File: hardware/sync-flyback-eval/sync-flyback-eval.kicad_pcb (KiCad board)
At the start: 2 copper layers, 90.8 x 46.4 mm, 97 parts, among them J1 RJ45_LED_Shielded, Q1 SiR422DP, Q2 Si7898DP, Q3 MMDT3906, T1 PoE_Transformer, T2 Pulse_Transformer, U1 TPS23754PWPR, U2 TCMT1107

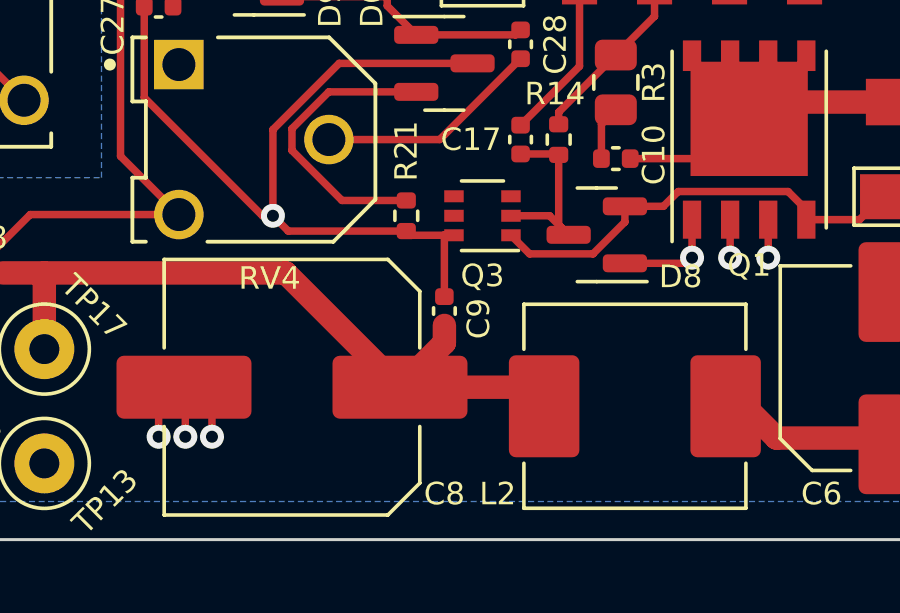
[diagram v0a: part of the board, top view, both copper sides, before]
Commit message: flyback: shift C9 to provide a bit more clearance
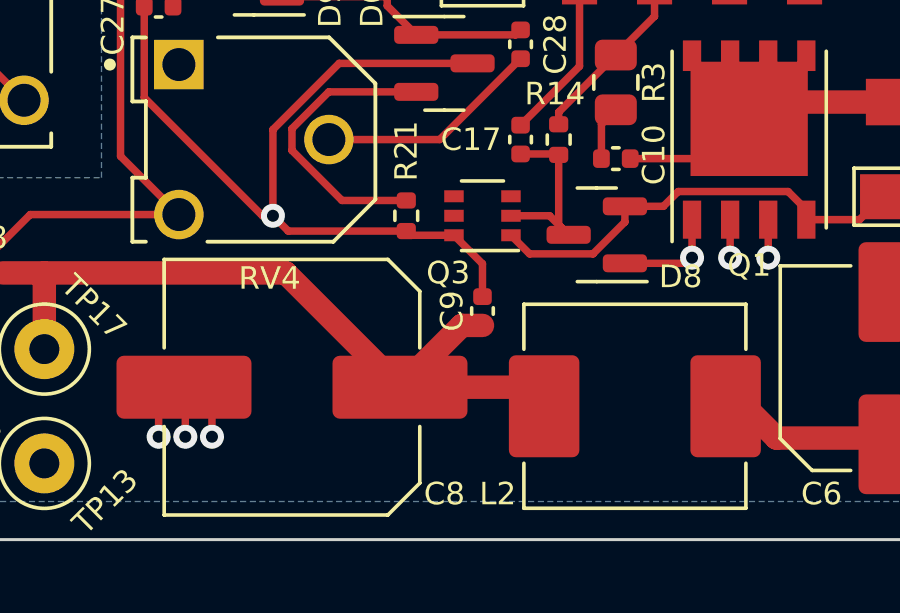
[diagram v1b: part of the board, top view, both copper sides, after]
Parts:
- moved C9 1.27 mm to (160.0, 113.0)
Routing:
- net Net-(C8-Pad1): track 24.8 -> 25.8 mm
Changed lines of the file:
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@@
   )
   (footprint "Capacitor_SMD:C_0402_1005Metric" (layer "F.Cu")
-    (at 158.75 113.03 90)
+    (at 160.02 113.03 90)
     (descr "Capacitor SMD 0402 (1005 Metric), square (rectangular) end terminal, IPC_7351 nominal, (Body size source: IPC-SM-782 page 76, https://www.pcb-3d.com/wordpress/wp-content/uploads/ipc-sm-782a_amendment_1_and_2.pdf), generated with kicad-footprint-generator")
     (tags "capacitor")
@@
     (property "Voltage" "16V")
     (attr smd)
-    (fp_text reference "C9" (at -0.254 1.143 90) (layer "F.SilkS")
+    (fp_text reference "C9" (at 0 -1.016 90) (layer "F.SilkS")
       (effects (font (size 0.75 0.75) (thickness 0.1)))
     )
@@
     (property "Sheetname" "")
     (attr smd)
-    (fp_text reference "Q3" (at 0 -2) (layer "F.SilkS")
+    (fp_text reference "Q3" (at 1.143 -1.905) (layer "F.SilkS")
       (effects (font (size 0.75 0.75) (thickness 0.1)))
     )
@@
   (segment (start 157.48 110.365) (end 153.545 110.365) (width 0.25) (layer "F.Cu") (net 5))
   (segment (start 164.135 100.235) (end 165.755 101.855) (width 0.25) (layer "F.Cu") (net 5))
+  (segment (start 160.02 112.55) (end 160.02 111.455) (width 0.25) (layer "F.Cu") (net 5))
   (segment (start 157.48 110.365) (end 157.62 110.505) (width 0.25) (layer "F.Cu") (net 5))
+  (segment (start 160.02 111.455) (end 159.07 110.505) (width 0.25) (layer "F.Cu") (net 5))
   (segment (start 148.745 102.87) (end 148.745 105.914622) (width 0.25) (layer "F.Cu") (net 5))
-  (segment (start 158.75 112.55) (end 158.75 110.49) (width 0.25) (layer "F.Cu") (net 5))
   (segment (start 157.62 110.505) (end 159.07 110.505) (width 0.25) (layer "F.Cu") (net 5))
   (segment (start 159.6875 104.775) (end 155.241418 104.775) (width 0.25) (layer "F.Cu") (net 5))
@@
   (segment (start 140.690028 85.09) (end 140.690028 83.57) (width 0.25) (layer "F.Cu") (net 63))
   (segment (start 144.160011 88.1888) (end 144.160011 87.391011) (width 0.25) (layer "F.Cu") (net 63))
-  (segment (start 157.27 115.57) (end 158.75 114.09) (width 0.781439) (layer "F.Cu") (net 64))
+  (segment (start 160.02 113.51) (end 159.33 113.51) (width 0.781439) (layer "F.Cu") (net 64))
+  (segment (start 159.33 113.51) (end 157.27 115.57) (width 0.781439) (layer "F.Cu") (net 64))
   (segment (start 145.415 114.3) (end 145.415 111.76) (width 0.781439) (layer "F.Cu") (net 64))
   (segment (start 153.46 111.76) (end 144.02 111.76) (width 0.781439) (layer "F.Cu") (net 64))
   (segment (start 157.27 115.57) (end 153.46 111.76) (width 0.781439) (layer "F.Cu") (net 64))
   (segment (start 157.27 115.57) (end 162.075 115.57) (width 0.781439) (layer "F.Cu") (net 64))
-  (segment (start 158.75 114.09) (end 158.75 113.51) (width 0.781439) (layer "F.Cu") (net 64))
   (segment (start 116.715 77.47) (end 116.715 78.74) (width 0.25) (layer "F.Cu") (net 65))
   (segment (start 116.73 77.47) (end 118.11 77.47) (width 0.25) (layer "F.Cu") (net 65))

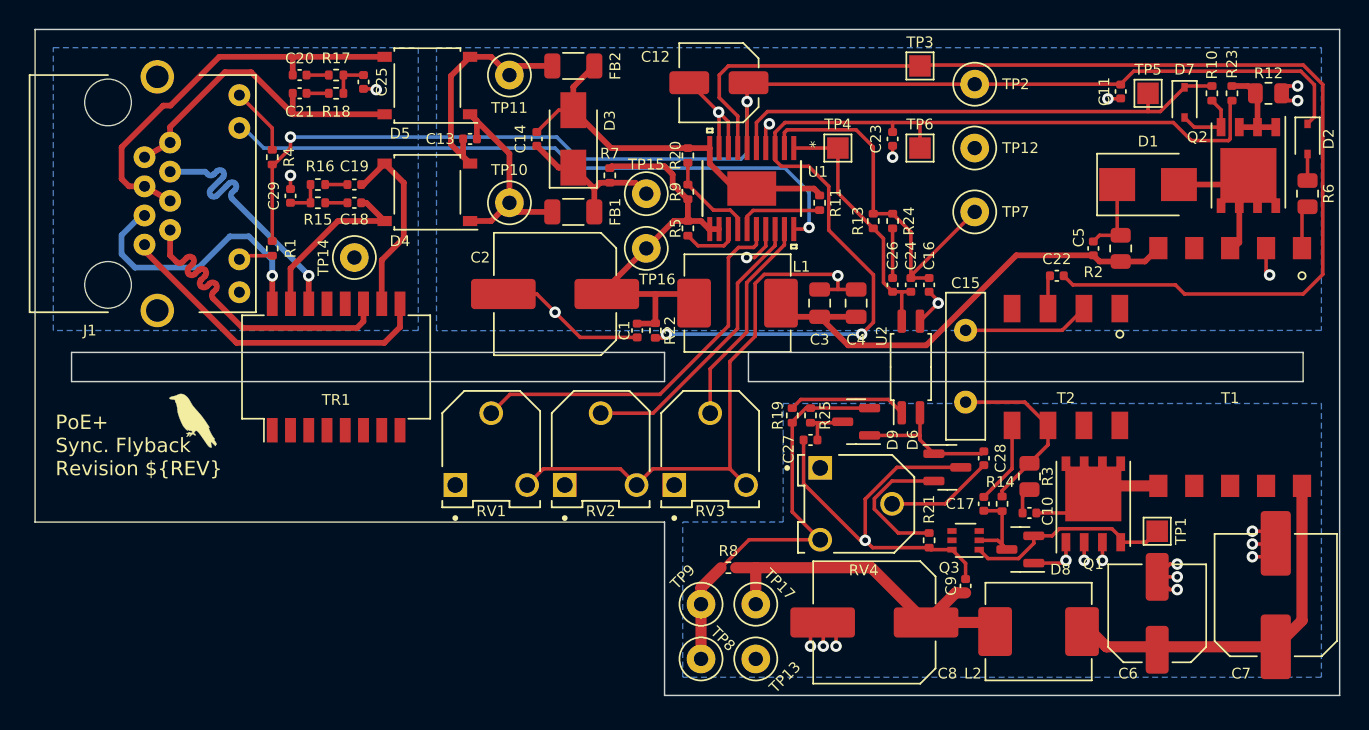
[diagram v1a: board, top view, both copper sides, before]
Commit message: flyback: update layout with new footprints
This ended up shuffling quite a bit around. I got rid of the notch in
the board, since that space is now needed. A lot of this will be
simplified once the varistors are no longer needed.
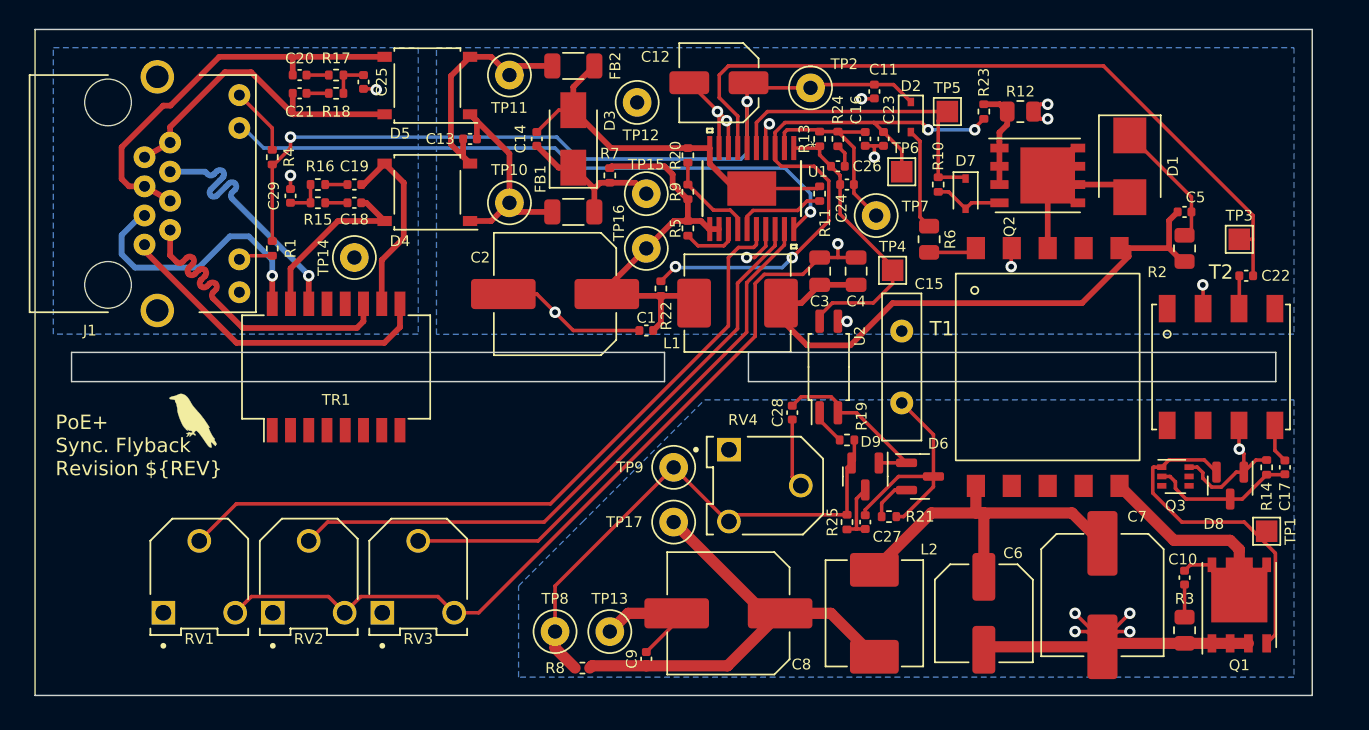
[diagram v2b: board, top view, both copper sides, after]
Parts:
- T1: footprint common:POE_EP13 -> common:WE-PoE+
- T2: footprint common:GDTI_EP7 -> common:WE-GDTI
- moved D2 27.7 mm to (156.2, 80.4)
- moved R6 26.5 mm to (157.5, 88.9)
- moved TP3 25.3 mm to (179.1, 88.9)
- moved TP12 23.7 mm to (137.2, 79.4)
- moved C9 22.8 mm to (137.8, 118.1)
- moved RV2 22.2 mm to (114.3, 112.4)
- moved RV3 22.2 mm to (121.9, 112.4)
- moved RV1 22.2 mm to (106.7, 112.4)
- moved C17 21.1 mm to (182.2, 104.8)
- moved R10 20.1 mm to (158.1, 85.1)
- moved R14 18.6 mm to (181.0, 104.8)
- moved R23 17.3 mm to (161.3, 80.0)
- moved R12 17.3 mm to (163.8, 80.0)
- moved C11 17.1 mm to (153.7, 78.6)
- moved D7 16.5 mm to (160.0, 85.7)
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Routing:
- net /VC: track 91.4 -> 59.5 mm
- net Net-(C22-Pad2): track 80.8 -> 52.5 mm
- net Net-(C23-Pad2): track 70.5 -> 42.3 mm, vias 2 -> 4
- net /BLNK: track 20.0 -> 44.0 mm
- net /DT: track 27.2 -> 51.2 mm
- net /FRS: track 15.0 -> 37.2 mm
- net Net-(D7-Pad1): track 35.8 -> 22.0 mm
- net /VB: track 26.4 -> 13.6 mm
- net Net-(C3-Pad1): track 31.8 -> 41.4 mm
- net Net-(D8-Pad2): track 14.7 -> 23.6 mm
- net GNDA: track 81.7 -> 90.0 mm, vias 11 -> 13
- net +12V: track 29.4 -> 36.5 mm
- net Net-(D6-Pad2): track 9.88 -> 3.05 mm
- net Net-(R19-Pad2): track 8.25 -> 1.97 mm
- net Net-(C10-Pad2): track 9.27 -> 15.4 mm
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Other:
- board size 90.8 x 46.4 mm -> 88.9 x 46.4 mm
